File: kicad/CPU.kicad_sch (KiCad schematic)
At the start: 37 parts, among them J1 Conn_ARM_SWD_TagConnect_TC203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, J2 Screw_Terminal_01x03, J3 Screw_Terminal_01x03, SW1 SW_Push, U7 STM32F303CBTx, Y1 8 MHz

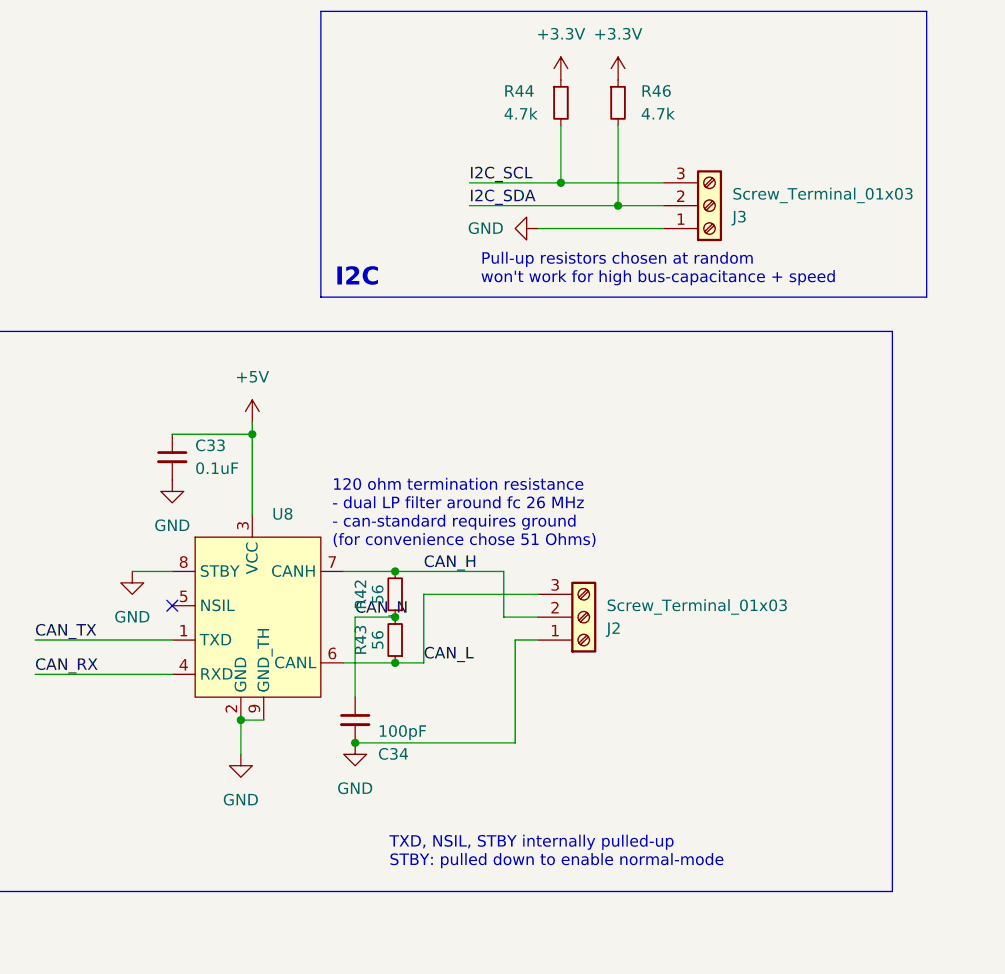
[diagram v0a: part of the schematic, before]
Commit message: [kicad] Done first set of footprint checks, adapted connector to regular phoenix connector, found 3d models for everything but button [scripts] Checked resonator calculation [simulations] Checked bootstrap simulation [cubemx] Added extra GPIO-input + checked cpu pins
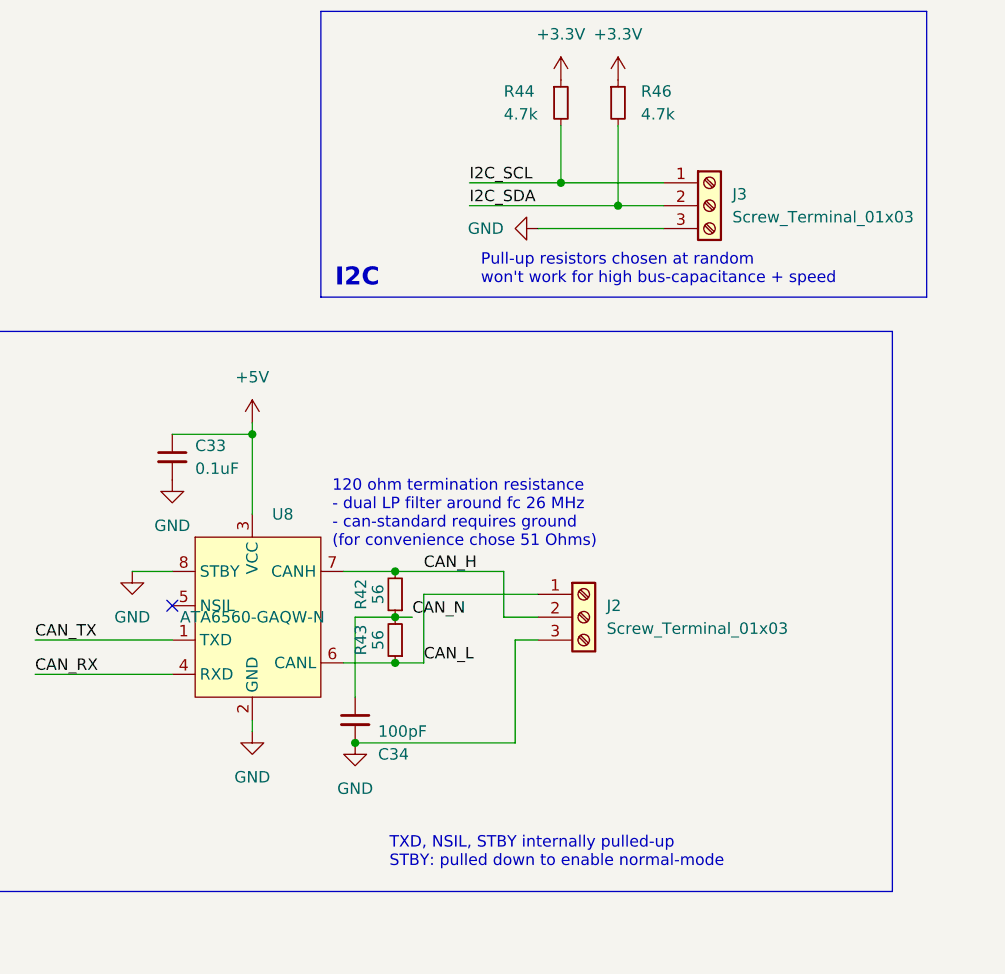
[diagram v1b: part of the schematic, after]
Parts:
- C23, C24, C25, C26, C27, C28, C30, C33: footprint Resistor_SMD:R_0402_1005Metric -> Capacitor_SMD:C_0402_1005Metric
- J2: footprint bldc:Ningbo-Kangnex-Elec_3x1-WJ500V-5.08-3P -> TerminalBlock_Phoenix:TerminalBlock_Phoenix_MPT-0,5-3-2.54_1x03_P2.54mm_Horizontal; MFR.Part WJ500V-5.08-3P -> 1725669; jlcpcb C72334 -> C5288763
- J3: footprint TerminalBlock:TerminalBlock_bornier-3_P5.08mm -> TerminalBlock_Phoenix:TerminalBlock_Phoenix_MPT-0,5-3-2.54_1x03_P2.54mm_Horizontal; MFR.Part WJ500V-5.08-3P -> 1725669; jlcpcb C72334 -> C5288763
- R45: JLCPCB C17168 -> (none); jlcpcb (none) -> C17168
- U7: MFR.Part (none) -> STM32F303CBT6; jlcpcb (none) -> C108516
- U8: value ~ -> ATA6560-GAQW-N; footprint bldc:MICROCHIP_CAN_ATA6560-GAQW-N -> bldc:SOIC-8-N8_3.9x4.9mm_P1.27mm
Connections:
- net CAN_L: now also J2.1 (Pin_1); no longer J2.3 (Pin_3)
- net GND: now also J2.3 (Pin_3), J3.3 (Pin_3); no longer J2.1 (Pin_1), J3.1 (Pin_1), U8.9 (GND_TH)
- net I2C_SCL: now also J3.1 (Pin_1); no longer J3.3 (Pin_3)

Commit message: [kicad] Rechecked all footprints and components requirements | TODO: think about replacing the ESD package with something else [simulations] Checked simulations of buck converter with reality
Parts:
- C22: MFR.Part (none) -> CL10A475KO8NNNC
- C23, C24, C25, C26, C27, C28, C30, C33: MFR.Part (none) -> CL05B104KB54PNC
- C32: footprint Resistor_SMD:R_0402_1005Metric -> Capacitor_SMD:C_0402_1005Metric; MFR.Part (none) -> CL05B104KB54PNC
- R35, R37, R38: MFR.Part (none) -> 0603WAF3302T5E
- R36: MFR.Part (none) -> 0805W8F1501T5E
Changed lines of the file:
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@@
+      (effects (font (size 1.27 1.27)) hide)
+    )
+    (property "MFR.Part" "CL05B104KB54PNC" (at 29.21 76.2 0)
       (effects (font (size 1.27 1.27)) hide)
     )
@@
       (effects (font (size 1.27 1.27)) (justify left))
     )
-    (property "Footprint" "Resistor_SMD:R_0402_1005Metric" (at 107.95 46.99 0)
+    (property "Footprint" "Capacitor_SMD:C_0402_1005Metric" (at 107.95 46.99 0)
       (effects (font (size 1.27 1.27)) hide)
     )
@@
     )
     (property "jlcpcb" "C307331" (at 107.95 46.99 0)
+      (effects (font (size 1.27 1.27)) hide)
+    )
+    (property "MFR.Part" "CL05B104KB54PNC" (at 107.95 46.99 0)
       (effects (font (size 1.27 1.27)) hide)
     )
@@
       (effects (font (size 1.27 1.27)) hide)
     )
+    (property "MFR.Part" "CL05B104KB54PNC" (at 63.5 76.2 0)
+      (effects (font (size 1.27 1.27)) hide)
+    )
     (pin "1")
     (pin "2")
@@
       (effects (font (size 1.27 1.27)) hide)
     )
+    (property "MFR.Part" "CL05B104KB54PNC" (at 200.66 114.3 0)
+      (effects (font (size 1.27 1.27)) hide)
+    )
     (pin "1")
     (pin "2")
@@
       (effects (font (size 1.27 1.27)) hide)
     )
+    (property "MFR.Part" "CL05B104KB54PNC" (at 38.1 76.2 0)
+      (effects (font (size 1.27 1.27)) hide)
+    )
     (pin "1")
     (pin "2")
@@
       (effects (font (size 1.27 1.27)) hide)
     )
+    (property "MFR.Part" "CL05B104KB54PNC" (at 43.18 121.285 0)
+      (effects (font (size 1.27 1.27)) hide)
+    )
     (pin "1")
     (pin "2")
@@
     )
     (property "jlcpcb" "C19666" (at 20.32 76.2 0)
+      (effects (font (size 1.27 1.27)) hide)
+    )
+    (property "MFR.Part" "CL10A475KO8NNNC" (at 20.32 76.2 0)
       (effects (font (size 1.27 1.27)) hide)
     )
@@
       (effects (font (size 1.27 1.27)) hide)
     )
+    (property "MFR.Part" "0603WAF3302T5E" (at 38.1 40.64 0)
+      (effects (font (size 1.27 1.27)) hide)
+    )
     (pin "2")
     (pin "1")
@@
       (effects (font (size 1.27 1.27)) hide)
     )
+    (property "MFR.Part" "0603WAF3302T5E" (at 62.23 29.21 0)
+      (effects (font (size 1.27 1.27)) hide)
+    )
     (pin "2")
     (pin "1")
@@
       (effects (font (size 1.27 1.27)) hide)
     )
+    (property "MFR.Part" "0603WAF3302T5E" (at 52.705 121.92 0)
+      (effects (font (size 1.27 1.27)) hide)
+    )
     (pin "2")
     (pin "1")
@@
       (effects (font (size 1.27 1.27)) hide)
     )
+    (property "MFR.Part" "CL05B104KB54PNC" (at 46.99 76.2 0)
+      (effects (font (size 1.27 1.27)) hide)
+    )
     (pin "1")
     (pin "2")
@@
       (effects (font (size 1.27 1.27)) hide)
     )
+    (property "MFR.Part" "CL05B104KB54PNC" (at 85.09 76.2 0)
+      (effects (font (size 1.27 1.27)) hide)
+    )
     (pin "1")
     (pin "2")
@@
     )
     (property "jlcpcb" "C4310" (at 38.1 118.11 0)
+      (effects (font (size 1.27 1.27)) hide)
+    )
+    (property "MFR.Part" "0805W8F1501T5E" (at 38.1 118.11 0)
       (effects (font (size 1.27 1.27)) hide)
     )
@@
       (effects (font (size 1.27 1.27)) hide)
     )
+    (property "MFR.Part" "CL05B104KB54PNC" (at 54.61 76.2 0)
+      (effects (font (size 1.27 1.27)) hide)
+    )
